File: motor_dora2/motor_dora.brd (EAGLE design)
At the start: 57.6 x 39.6 mm, 38 parts

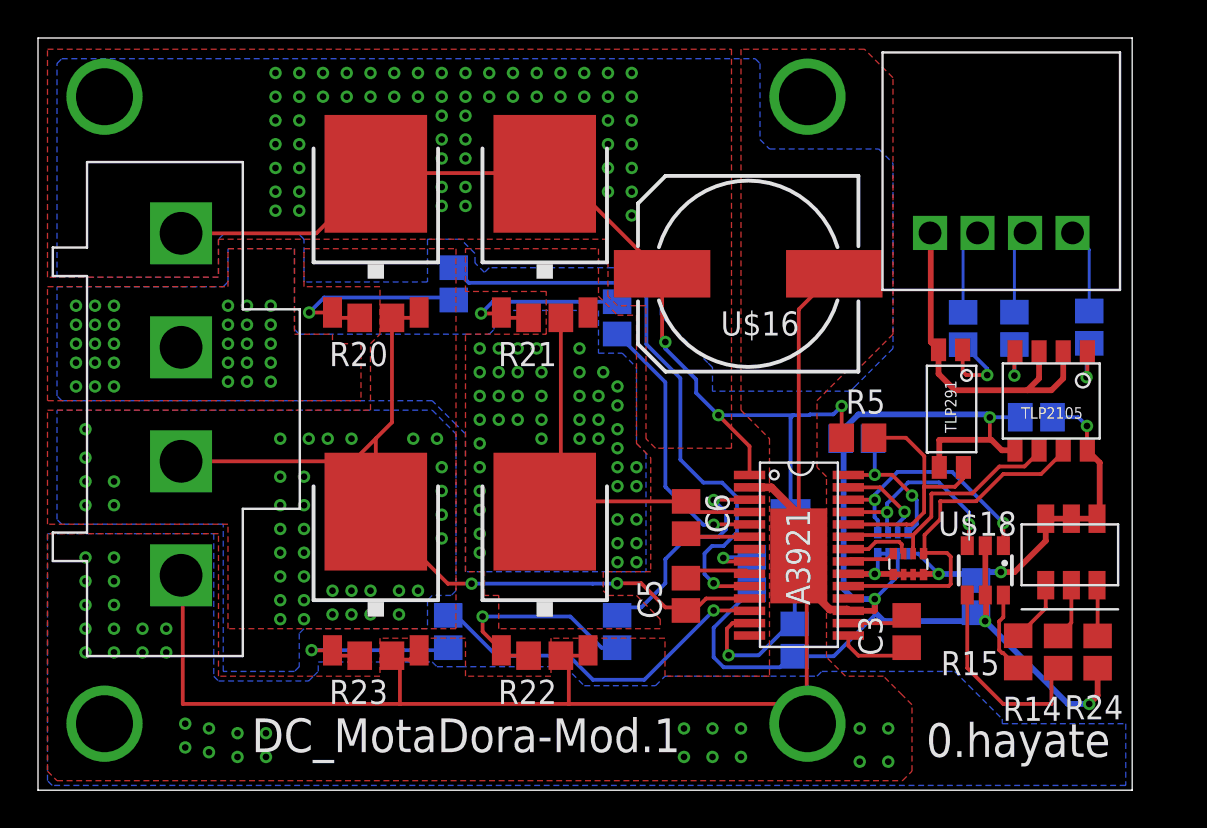
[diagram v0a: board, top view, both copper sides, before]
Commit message: ゲート駆動を調整
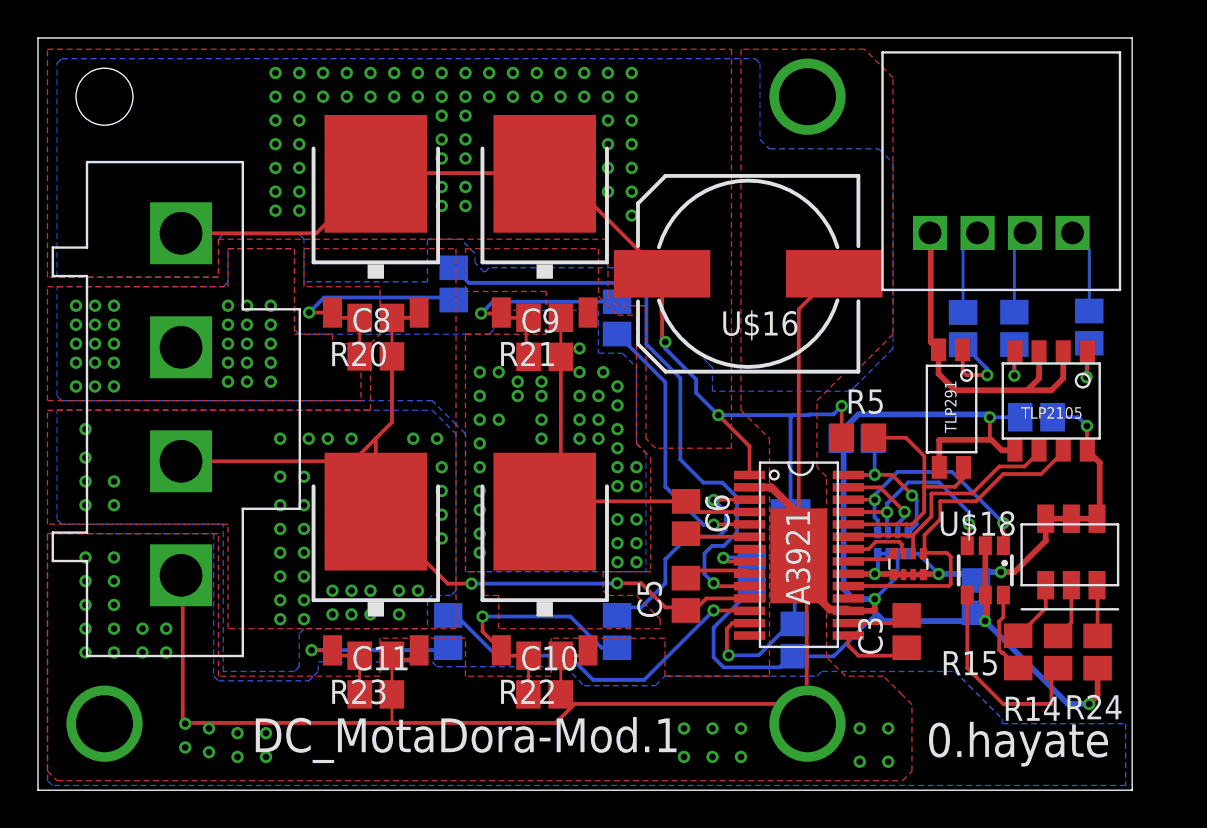
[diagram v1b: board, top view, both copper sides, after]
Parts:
- added C10, C11, C8, C9: (no value), rcl:C2012
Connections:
- net GND: now also C10.2, C11.2
- net N$24: now also C8.1
- net N$25: now also C9.1
- net N$26: now also C11.1
- net N$27: now also C10.1
- net SA: now also C8.2
- net SB: now also C9.2
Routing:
- net GND: track 146.4 -> 150.1 mm
- net N$25: track 10.3 -> 12.4 mm
- net N$27: track 11.5 -> 13.5 mm
- net N$26: track 10.2 -> 12.2 mm
- net N$24: track 11.0 -> 13.1 mm
- net VCC: vias 65 -> 64
- net SB: vias 76 -> 70

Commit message: pwm入力をプルダウンにした
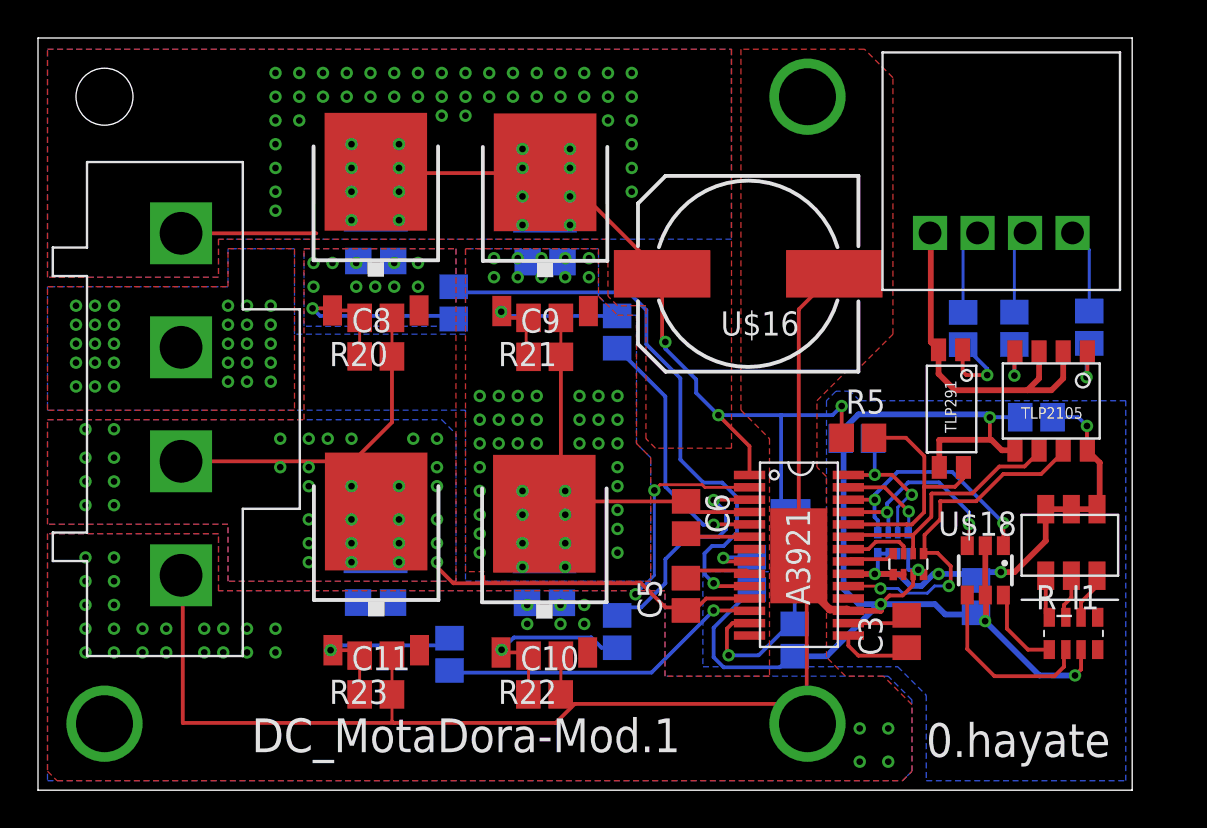
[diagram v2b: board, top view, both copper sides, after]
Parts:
- removed R14, R15, R24: 1k, rcl:R2012
- added R_I1: 1k, user_rcl:0603X4RESISTOR
- added U$12, U$15, U$19, U$7: SBR10M100P5Q, user_diode:POWERDI_5
- U$10, U$11, U$8, U$9: value NP52N06SLG -> IPD034N06N3G; device user:NP52N06SLG -> user_tr_fet_igbt:TO252
- moved U$9 20.0 mm to (26.7, 30.0)
- moved U$10 19.9 mm to (17.8, 12.2)
- moved R17 1.20 mm to (21.7, 7.15), turned to 90 degrees
- moved R16 1.00 mm to (21.9, 25.6)
- moved R19 0.75 mm to (30.5, 24.1)
- moved U$4 0.50 mm to (53.0, 11.3)
- moved U$11 0.11 mm to (26.6, 12.1)
- moved U$8 0.11 mm to (17.8, 30.1)
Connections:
- net GND: now also R_I1.3, U$10.PIN3, U$11.PIN3, U$12.1, U$12.2, U$5.5, U$5.6, U$6.8, U$7.1, U$7.2; no longer R24.1, U$11.PIN3_S, U$6.7, U$9.PIN3_S
- net N$14: now also R_I1.7, U$4.G_K; no longer R24.2, U$4.B_K
- net N$15: now also U$6.3; no longer U$6.4
- net N$18: now also R_I1.2; no longer R14.1
- net N$19: now also R_I1.8, U$4.R_K; no longer R15.1, U$18.6
- net N$20: now also R_I1.6, U$4.B_K; no longer R14.2, U$4.G_K
- net N$21: now also R_I1.1, U$18.6; no longer R15.2, U$4.R_K
- net N$24: now also U$8.PIN1; no longer U$8.PIN1_G
- net N$25: now also U$9.PIN1; no longer U$10.PIN1_G
- net N$26: now also U$10.PIN1; no longer U$9.PIN1_G
- net N$27: now also U$11.PIN1; no longer U$11.PIN1_G
- net N$5: now also U$6.4; no longer U$6.3
- net SA: now also U$10.PIN2, U$19.1, U$19.2, U$7.3, U$8.PIN3; no longer U$8.PIN3_S, U$9.PIN2_D
- net SB: now also U$11.PIN2, U$12.3, U$15.1, U$15.2, U$9.PIN3; no longer U$10.PIN3_S, U$11.PIN2_D
- net V5: now also U$6.7; no longer U$5.5, U$5.6, U$6.8
- net VCC: now also U$15.3, U$19.3, U$8.PIN2, U$9.PIN2; no longer U$10.PIN2_D, U$8.PIN2_D
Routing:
- net SA: track 45.0 -> 37.4 mm, vias 41 -> 43
- net GND: track 150.1 -> 157.1 mm, vias 39 -> 42
- net VCC: track 55.2 -> 50.6 mm
- net N$27: track 13.5 -> 10.3 mm
- net N$25: track 12.4 -> 10.2 mm
- net N$19: track 4.38 -> 2.27 mm
- net N$26: track 12.2 -> 10.3 mm
- net GLA: track 18.8 -> 17.2 mm
- net N$18: track 11.1 -> 9.67 mm
- net N$21: track 3.26 -> 4.53 mm
- net GHA: track 31.8 -> 30.8 mm
- net GHB: track 14.4 -> 13.6 mm
- net N$24: track 13.1 -> 12.4 mm
- net SB: track 21.8 -> 21.7 mm, vias 70 -> 79
- net N$29: vias 0 -> 2
